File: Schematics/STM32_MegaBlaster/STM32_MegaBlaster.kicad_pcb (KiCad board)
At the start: 2 copper layers, 138.4 x 91.4 mm, 91 parts, among them J1 SD_Card, J2 USB_B, J3 Barrel_Jack, J4 AMP_OUT, SW5 POWER, SW6 MUTE PSG, U1 BluePill_STM32F103C, U10 LD1117S33, U11 LM2596T-5, U12 I2C_OLED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

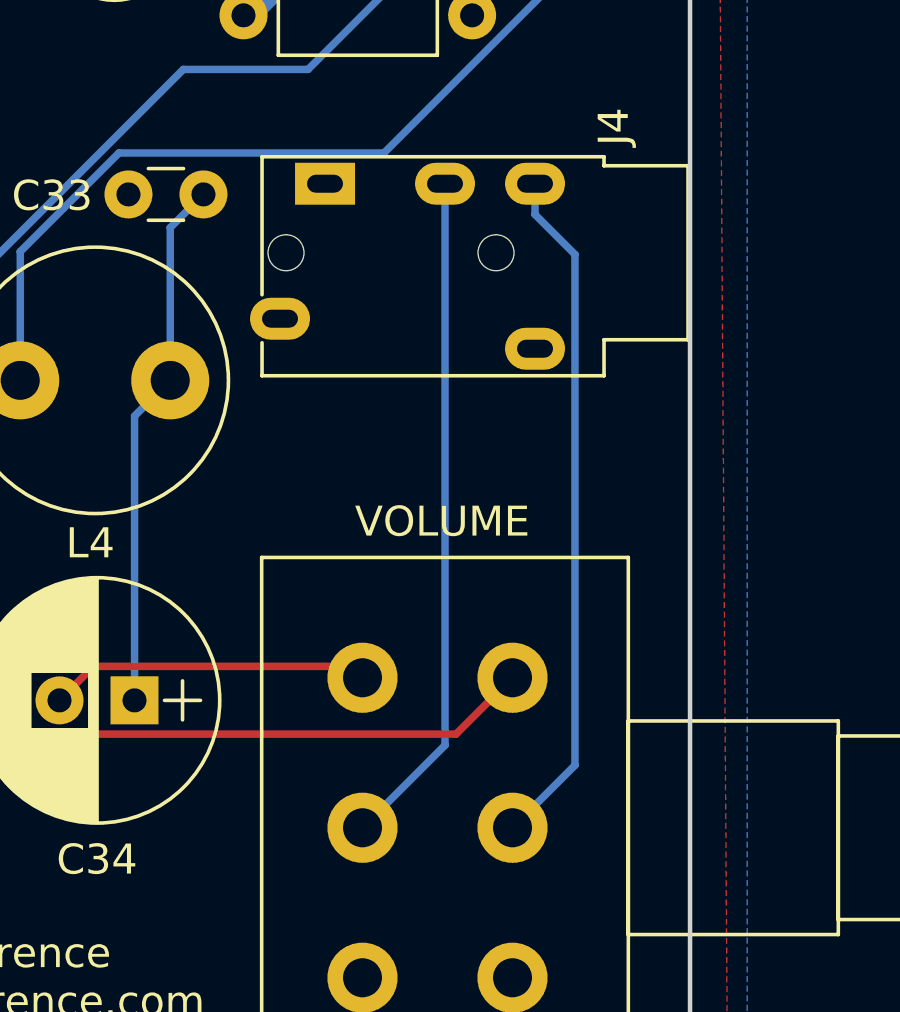
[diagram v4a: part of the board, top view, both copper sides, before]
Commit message: Corrected headphone jack
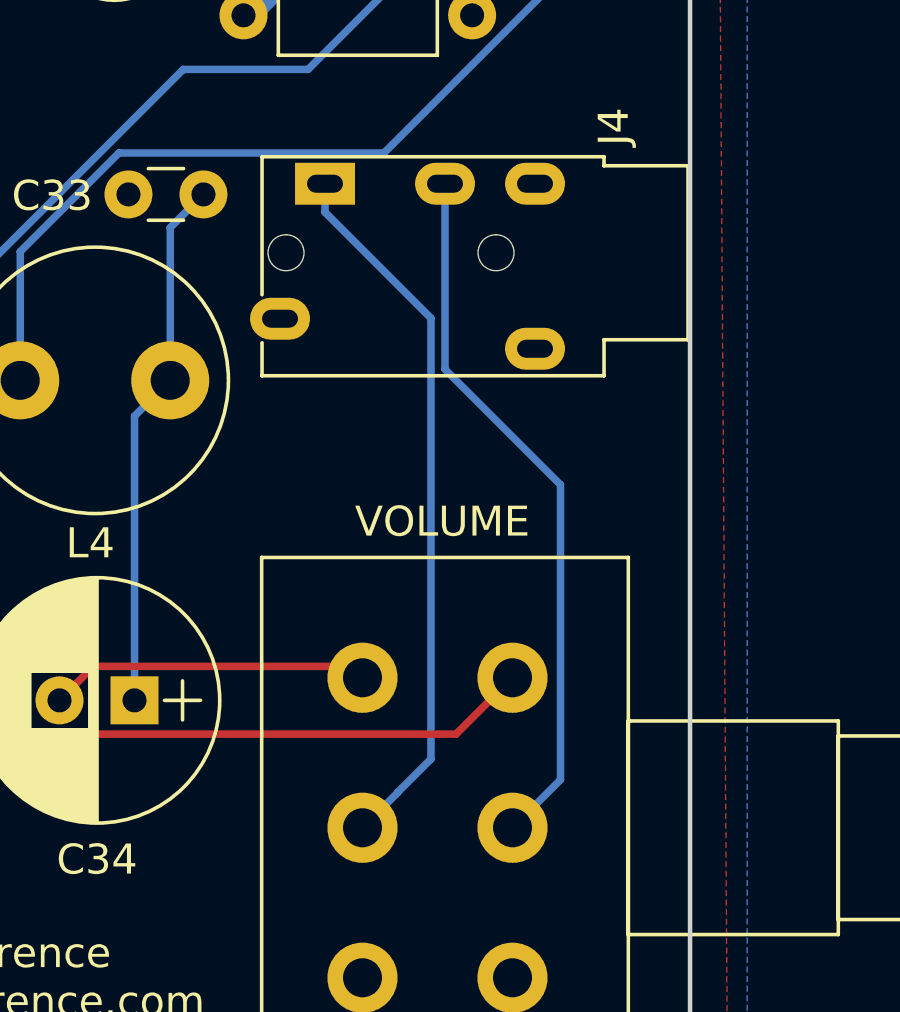
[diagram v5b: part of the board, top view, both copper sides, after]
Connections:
- J4 pad 1: GND -> Net-(J4-Pad2)
- J4 pad 2: Net-(J4-Pad2) -> Net-(J4-Pad3)
- J4 pad 3: Net-(J4-Pad3) -> GND
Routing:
- net Net-(J4-Pad2): track 22.6 -> 23.9 mm
- net Net-(J4-Pad3): track 22.9 -> 23.7 mm
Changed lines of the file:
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@@
     (thickness 1.6)
     (drawings 25)
-    (tracks 928)
+    (tracks 932)
     (zones 0)
     (modules 91)
@@
     (pad 4 thru_hole oval (at 4.5 1.5 180) (size 2 1.4) (drill oval 1.2 0.6) (layers *.Cu *.Mask))
     (pad 1 thru_hole rect (at 0 0 180) (size 2 1.4) (drill oval 1.2 0.6) (layers *.Cu *.Mask)
-      (net 4 GND))
-    (pad 2 thru_hole oval (at 0 -4 180) (size 2 1.4) (drill oval 1.2 0.6) (layers *.Cu *.Mask)
       (net 111 "Net-(J4-Pad2)"))
-    (pad 3 thru_hole oval (at 0 -7 180) (size 2 1.4) (drill oval 1.2 0.6) (layers *.Cu *.Mask)
+    (pad 2 thru_hole oval (at 0 -4 180) (size 2 1.4) (drill oval 1.2 0.6) (layers *.Cu *.Mask)
       (net 110 "Net-(J4-Pad3)"))
+    (pad 3 thru_hole oval (at 0 -7 180) (size 2 1.4) (drill oval 1.2 0.6) (layers *.Cu *.Mask)
+      (net 4 GND))
     (pad "" np_thru_hole circle (at 2.3 -5.7 180) (size 1.2 1.2) (drill 1.2) (layers *.Cu *.Mask))
     (pad "" np_thru_hole circle (at 2.3 1.3 180) (size 1.2 1.2) (drill 1.2) (layers *.Cu *.Mask))
@@
   (segment (start 111.2003 37.79) (end 111.2003 38.32) (width 0.25) (layer F.Cu) (net 97))
   (segment (start 111.2003 38.32) (end 113.665 40.7847) (width 0.25) (layer F.Cu) (net 97))
-  (segment (start 192.318 90.17) (end 192.318 91.1953) (width 0.25) (layer B.Cu) (net 110))
-  (segment (start 191.567 111.637) (end 193.6493 109.5547) (width 0.25) (layer B.Cu) (net 110))
-  (segment (start 193.6493 109.5547) (end 193.6493 92.5266) (width 0.25) (layer B.Cu) (net 110))
-  (segment (start 193.6493 92.5266) (end 192.318 91.1953) (width 0.25) (layer B.Cu) (net 110))
-  (segment (start 186.567 111.637) (end 189.318 108.886) (width 0.25) (layer B.Cu) (net 111))
-  (segment (start 189.318 108.886) (end 189.318 90.17) (width 0.25) (layer B.Cu) (net 111))
+  (segment (start 193.167 110.037) (end 193.167 100.203) (width 0.25) (layer B.Cu) (net 110))
+  (segment (start 191.567 111.637) (end 193.167 110.037) (width 0.25) (layer B.Cu) (net 110))
+  (segment (start 189.318 96.354) (end 189.318 90.17) (width 0.25) (layer B.Cu) (net 110))
+  (segment (start 193.167 100.203) (end 189.318 96.354) (width 0.25) (layer B.Cu) (net 110))
+  (segment (start 187.736999 110.467001) (end 187.736999 110.459001) (width 0.25) (layer B.Cu) (net 111))
+  (segment (start 186.567 111.637) (end 187.736999 110.467001) (width 0.25) (layer B.Cu) (net 111))
+  (segment (start 187.736999 110.459001) (end 188.849 109.347) (width 0.25) (layer B.Cu) (net 111))
+  (segment (start 185.318 91.12) (end 185.318 90.17) (width 0.25) (layer B.Cu) (net 111))
+  (segment (start 188.849 94.651) (end 185.318 91.12) (width 0.25) (layer B.Cu) (net 111))
+  (segment (start 188.849 109.347) (end 188.849 94.651) (width 0.25) (layer B.Cu) (net 111))
   (segment (start 117.8 61.935) (end 117.8 63.308) (width 0.25) (layer F.Cu) (net 112))
   (segment (start 117.8 63.308) (end 118.6895 64.1975) (width 0.25) (layer F.Cu) (net 112))

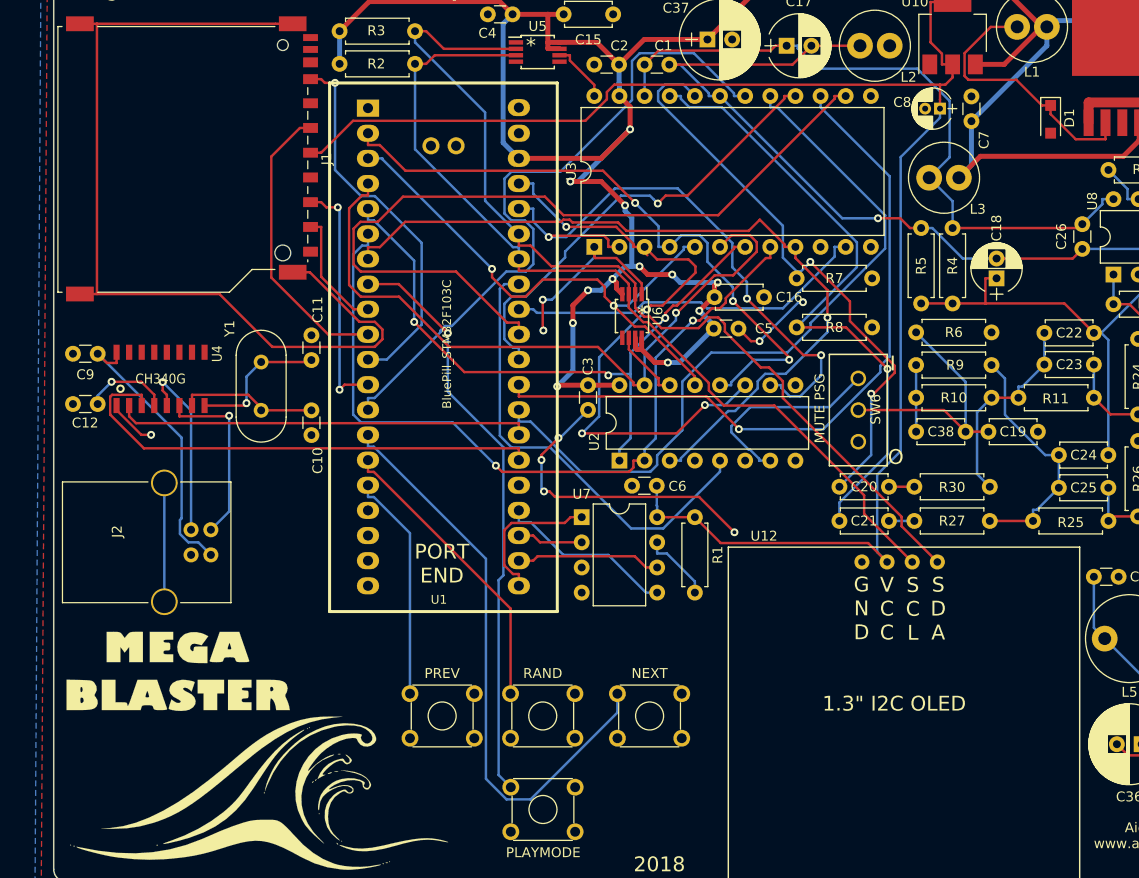
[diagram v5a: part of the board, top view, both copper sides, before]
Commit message: Changed diode to more friendly package, moved OLED I2C lines far away from mixer circuit
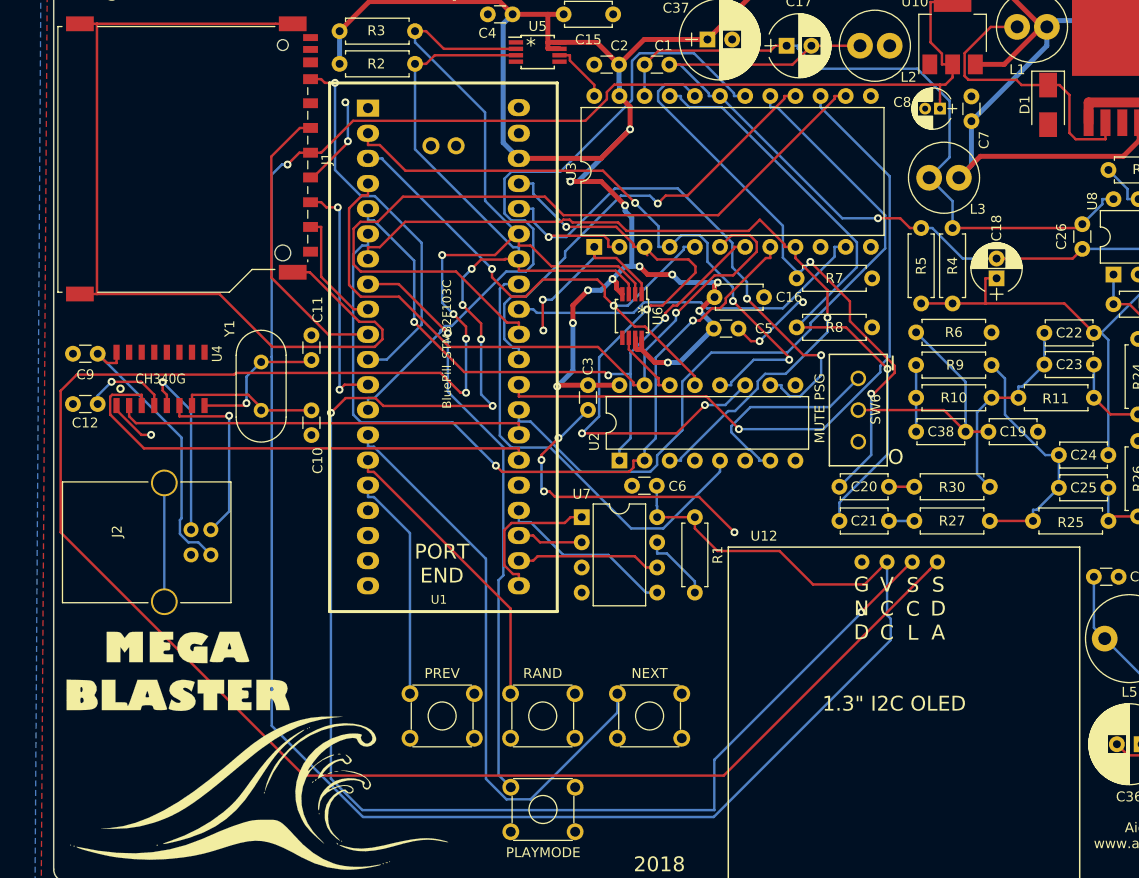
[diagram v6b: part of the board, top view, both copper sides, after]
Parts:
- D1: footprint Diodes_SMD:D_SOD-123F -> Diodes_SMD:D_SMA
- moved D1 1.48 mm to (159.5, 42.8)
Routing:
- net I2C_SDA: track 96.8 -> 239.6 mm, vias 0 -> 4
- net I2C_SCL: track 91.0 -> 197.6 mm, vias 0 -> 6
- net +3V3: track 159.4 -> 255.4 mm, vias 0 -> 1
- net GND: track 64.2 -> 73.6 mm, vias 9 -> 11
- net Net-(D1-Pad1): track 27.8 -> 29.5 mm
